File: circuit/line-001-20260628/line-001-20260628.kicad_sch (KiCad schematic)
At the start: 130 parts, among them J1 Conn_01x02_Pin, J2 Conn_01x02_Pin

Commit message: Update ライン基板の回路図を更新
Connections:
- net linesig1 renamed linesig1_{raw}
- net linesig10 renamed linesig10_{raw}
- net linesig11 renamed linesig11_{raw}
- net linesig12 renamed linesig12_{raw}
- net linesig13 renamed linesig13_{raw}
- net linesig14 renamed linesig14_{raw}
- net linesig15 renamed linesig15_{raw}
- net linesig16 renamed linesig16_{raw}
- net linesig17 renamed linesig17_{raw}
- net linesig18 renamed linesig18_{raw}
- net linesig19 renamed linesig19_{raw}
- net linesig2 renamed linesig2_{raw}
- net linesig20 renamed linesig20_{raw}
- net linesig21 renamed linesig21_{raw}
- net linesig22 renamed linesig22_{raw}
- net linesig23 renamed linesig23_{raw}
- net linesig24 renamed linesig24_{raw}
- net linesig25 renamed linesig25_{raw}
- net linesig26 renamed linesig26_{raw}
- net linesig27 renamed linesig27_{raw}
- net linesig28 renamed linesig28_{raw}
- net linesig29 renamed linesig29_{raw}
- net linesig3 renamed linesig3_{raw}
- net linesig30 renamed linesig30_{raw}
- net linesig31 renamed linesig31_{raw}
- net linesig32 renamed linesig32_{raw}
- net linesig4 renamed linesig4_{raw}
- net linesig5 renamed linesig5_{raw}
- net linesig6 renamed linesig6_{raw}
- net linesig7 renamed linesig7_{raw}
- net linesig8 renamed linesig8_{raw}
- net linesig9 renamed linesig9_{raw}

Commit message: Update ラインセンサ基板にコンパレーターを追加（シンボルを作成）
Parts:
- added C1, C2, C3, C4: 10u, symbol Device:C
- added D63, D64, D65, D68: LED, symbol Device:LED
- added D69, D70, D71, D72: D_Photo, symbol Device:D_Photo
- added R63, R64, R65, R68: 10k, symbol Device:R
- added R69, R70, R71, R72: 75, symbol Device:R
- added R73, R74, R75, R76: 1k, symbol Device:R
- added U1, U10, U11, U12, U13, U14, U15, U16, U2, U3, U4, U5, U6, U7, U8, U9: LM339DR, symbol @Thrive_symbol_line:LM393DR
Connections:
- net +5V_{Line}: now also D69.2 (A), D70.2 (A), D71.2 (A), D72.2 (A), R69.2, R70.2, R71.2, R72.2, U1.8 (V_{CC}), U10.8 (V_{CC}), U11.8 (V_{CC}), U12.8 (V_{CC}), U13.8 (V_{CC}), U14.8 (V_{CC}), U15.8 (V_{CC}), U16.8 (V_{CC}), U2.8 (V_{CC}), U3.8 (V_{CC}), U4.8 (V_{CC}), U5.8 (V_{CC}), U6.8 (V_{CC}), U7.8 (V_{CC}), U8.8 (V_{CC}), U9.8 (V_{CC})
- net GND: now also C1.2, C2.2, C3.2, C4.2, D63.1 (K), D64.1 (K), D65.1 (K), D68.1 (K), R63.1, R64.1, R65.1, R68.1, U1.4 (GND), U10.4 (GND), U11.4 (GND), U12.4 (GND), U13.4 (GND), U14.4 (GND), U15.4 (GND), U16.4 (GND), U2.4 (GND), U3.4 (GND), U4.4 (GND), U5.4 (GND), U6.4 (GND), U7.4 (GND), U8.4 (GND), U9.4 (GND)
- net linesig10_{raw}: now also U5.5 (2_{IN+})
- net linesig11_{raw}: now also U6.3 (1_{IN+})
- net linesig12_{raw}: now also U6.5 (2_{IN+})
- net linesig13_{raw}: now also U7.3 (1_{IN+})
- net linesig14_{raw}: now also U7.5 (2_{IN+})
- net linesig15_{raw}: now also U8.3 (1_{IN+})
- net linesig16_{raw}: now also U8.5 (2_{IN+})
- net linesig17_{raw}: now also U9.3 (1_{IN+})
- net linesig18_{raw}: now also U9.5 (2_{IN+})
- net linesig19_{raw}: now also U10.3 (1_{IN+})
- net linesig1_{raw}: now also U1.3 (1_{IN+})
- net linesig20_{raw}: now also U10.5 (2_{IN+})
- net linesig21_{raw}: now also U11.3 (1_{IN+})
- net linesig22_{raw}: now also U11.5 (2_{IN+})
- net linesig23_{raw}: now also U12.3 (1_{IN+})
- net linesig24_{raw}: now also U12.5 (2_{IN+})
- net linesig25_{raw}: now also U13.3 (1_{IN+})
- net linesig26_{raw}: now also U13.5 (2_{IN+})
- net linesig27_{raw}: now also U14.3 (1_{IN+})
- net linesig28_{raw}: now also U14.5 (2_{IN+})
- net linesig29_{raw}: now also U15.3 (1_{IN+})
- net linesig2_{raw}: now also U1.5 (2_{IN+})
- net linesig30_{raw}: now also U15.5 (2_{IN+})
- net linesig31_{raw}: now also U16.3 (1_{IN+})
- net linesig32_{raw}: now also U16.5 (2_{IN+})
- net linesig3_{raw}: now also U2.3 (1_{IN+})
- net linesig4_{raw}: now also U2.5 (2_{IN+})
- net linesig5_{raw}: now also U3.3 (1_{IN+})
- net linesig6_{raw}: now also U3.5 (2_{IN+})
- net linesig7_{raw}: now also U4.3 (1_{IN+})
- net linesig8_{raw}: now also U4.5 (2_{IN+})
- net linesig9_{raw}: now also U5.3 (1_{IN+})
- new net: D63.2 (A), R69.1
- new net: D64.2 (A), R70.1
- new net: D65.2 (A), R71.1
- new net: D68.2 (A), R72.1
- new net boundary_{backleft_raw}: R75.1
- new net boundary_{backleft}: C3.1, R75.2, U10.2 (1_{IN-}), U10.6 (2_{IN-}), U11.2 (1_{IN-}), U11.6 (2_{IN-}), U12.2 (1_{IN-}), U12.6 (2_{IN-}), U9.2 (1_{IN-}), U9.6 (2_{IN-})
- new net boundary_{backright_raw}: R74.1
- new net boundary_{backright}: C2.1, R74.2, U5.2 (1_{IN-}), U5.6 (2_{IN-}), U6.2 (1_{IN-}), U6.6 (2_{IN-}), U7.2 (1_{IN-}), U7.6 (2_{IN-}), U8.2 (1_{IN-}), U8.6 (2_{IN-})
- new net boundary_{frontleft_raw}: R76.1
- new net boundary_{frontleft}: C4.1, R76.2, U13.2 (1_{IN-}), U13.6 (2_{IN-}), U14.2 (1_{IN-}), U14.6 (2_{IN-}), U15.2 (1_{IN-}), U15.6 (2_{IN-}), U16.2 (1_{IN-}), U16.6 (2_{IN-})
- new net boundary_{frontright_raw}: R73.1
- new net boundary_{frontright}: C1.1, R73.2, U1.2 (1_{IN-}), U1.6 (2_{IN-}), U2.2 (1_{IN-}), U2.6 (2_{IN-}), U3.2 (1_{IN-}), U3.6 (2_{IN-}), U4.2 (1_{IN-}), U4.6 (2_{IN-})
- new net linesig10_{digital}: U5.7 (2_{OUT})
- new net linesig11_{digital}: U6.1 (1_{OUT})
- new net linesig12_{digital}: U6.7 (2_{OUT})
- new net linesig13_{digital}: U7.1 (1_{OUT})
- new net linesig14_{digital}: U7.7 (2_{OUT})
- new net linesig15_{digital}: U8.1 (1_{OUT})
- new net linesig16_{digital}: U8.7 (2_{OUT})
- new net linesig17_{digital}: U9.1 (1_{OUT})
- new net linesig18_{digital}: U9.7 (2_{OUT})
- new net linesig19_{digital}: U10.1 (1_{OUT})
- new net linesig1_{digital}: U1.1 (1_{OUT})
- new net linesig20_{digital}: U10.7 (2_{OUT})
- new net linesig21_{digital}: U11.1 (1_{OUT})
- new net linesig22_{digital}: U11.7 (2_{OUT})
- new net linesig23_{digital}: U12.1 (1_{OUT})
- new net linesig24_{digital}: U12.7 (2_{OUT})
- new net linesig25_{digital}: U13.1 (1_{OUT})
- new net linesig26_{digital}: U13.7 (2_{OUT})
- new net linesig27_{digital}: U14.1 (1_{OUT})
- new net linesig28_{digital}: U14.7 (2_{OUT})
- new net linesig29_{digital}: U15.1 (1_{OUT})
- new net linesig2_{digital}: U1.7 (2_{OUT})
- new net linesig30_{digital}: U15.7 (2_{OUT})
- new net linesig31_{digital}: U16.1 (1_{OUT})
- new net linesig32_{digital}: U16.7 (2_{OUT})
- new net linesig33_{analog}: D69.1 (K), R63.2
- new net linesig34_{analog}: D70.1 (K), R64.2
- new net linesig35_{analog}: D71.1 (K), R65.2
- new net linesig36_{analog}: D72.1 (K), R68.2
- new net linesig3_{digital}: U2.1 (1_{OUT})
- new net linesig4_{digital}: U2.7 (2_{OUT})
- new net linesig5_{digital}: U3.1 (1_{OUT})
- new net linesig6_{digital}: U3.7 (2_{OUT})
- new net linesig7_{digital}: U4.1 (1_{OUT})
- new net linesig8_{digital}: U4.7 (2_{OUT})
- new net linesig9_{digital}: U5.1 (1_{OUT})
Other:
- moved on the sheet: J1, J2

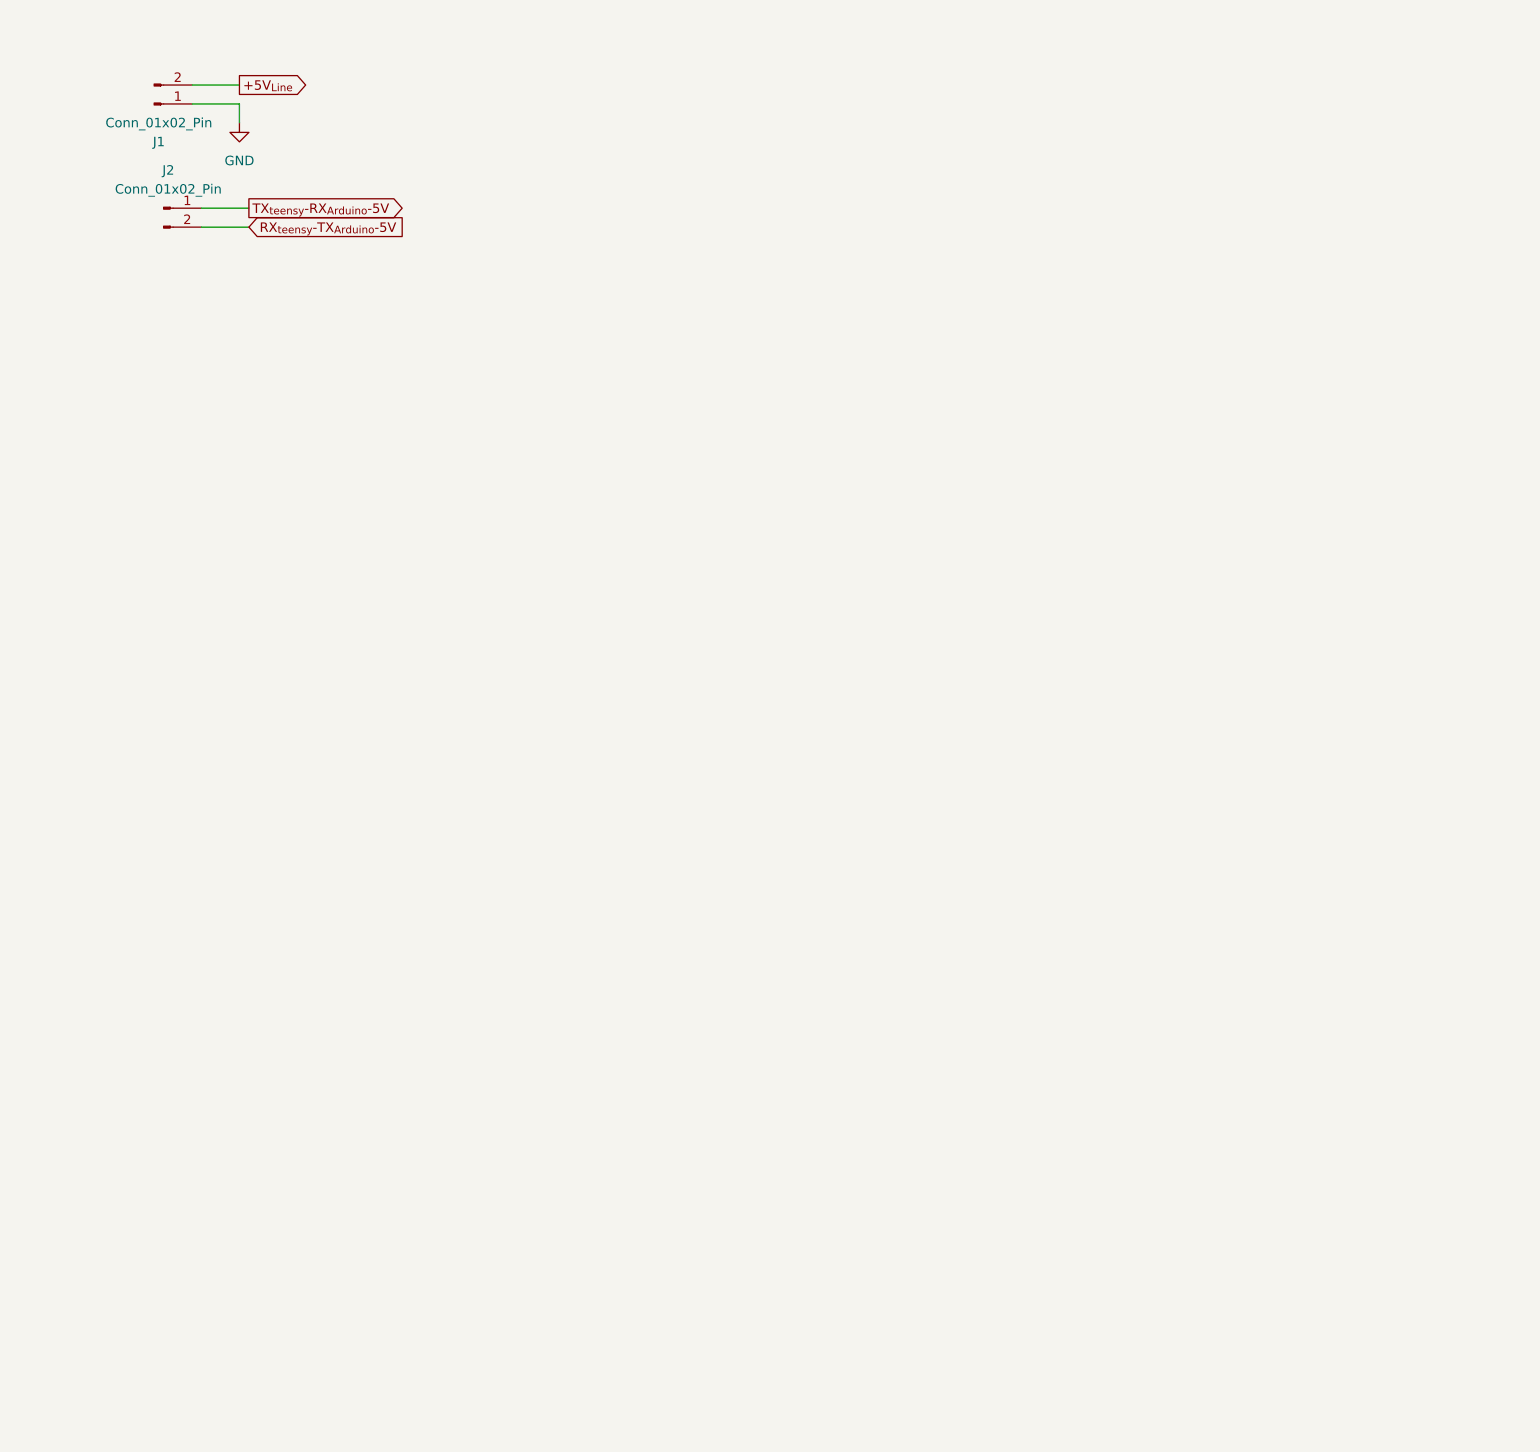
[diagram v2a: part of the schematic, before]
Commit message: Update ラインセンサ基板の回路図を更新
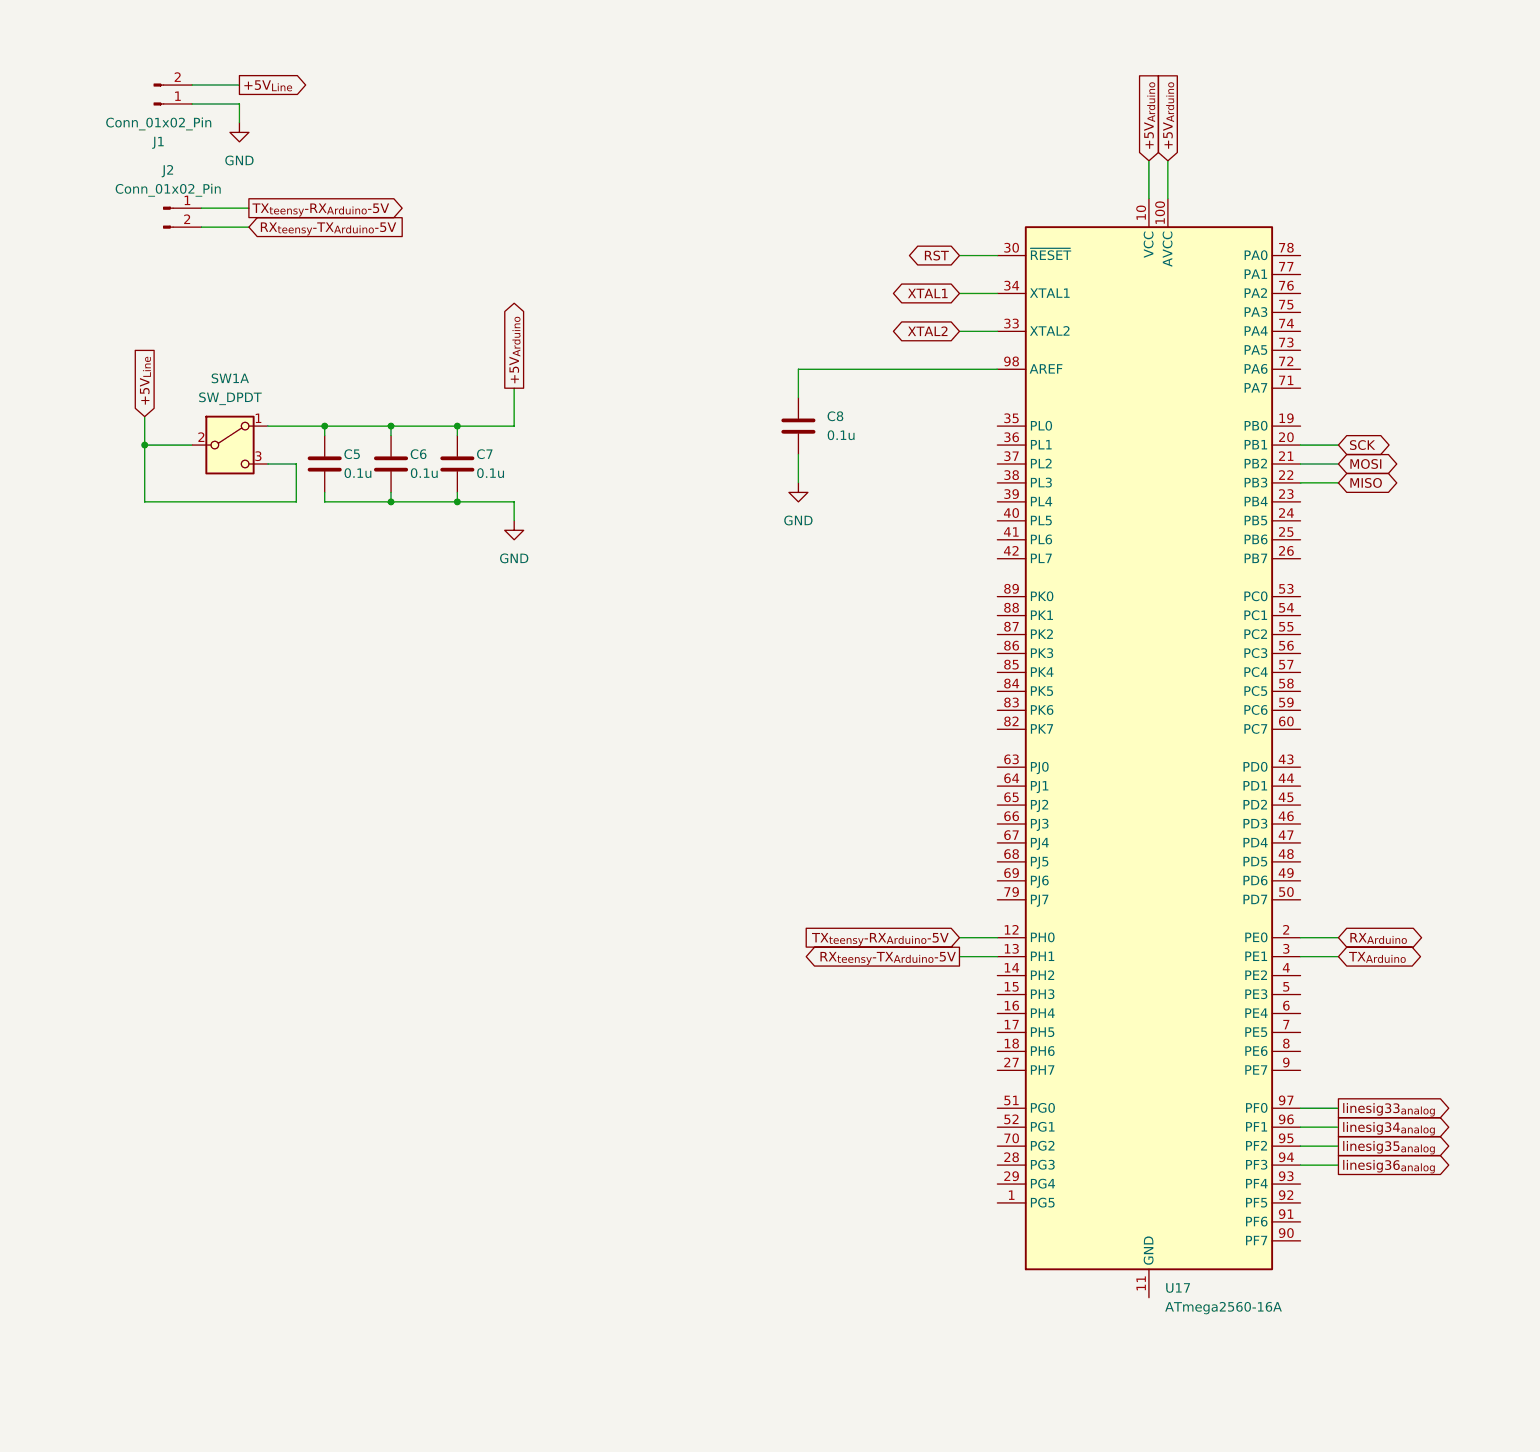
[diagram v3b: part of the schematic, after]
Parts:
- added C5, C6, C7, C8: 0.1u, symbol Device:C
- added SW1: SW_DPDT, symbol Switch:SW_DPDT_x2
- added U17: ATmega2560-16A, Package_QFP:TQFP-100_14x14mm_P0.5mm, symbol MCU_Microchip_ATmega:ATmega2560-16A
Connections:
- net +5V_{Line}: now also SW1.2 (B), SW1.3 (C)
- net GND: now also C5.2, C6.2, C7.2, C8.2
- net RX_{teensy}-TX_{Arduino}-5V: now also U17.13 (PH1)
- net TX_{teensy}-RX_{Arduino}-5V: now also U17.12 (PH0)
- net linesig33_{analog}: now also U17.97 (PF0)
- net linesig34_{analog}: now also U17.96 (PF1)
- net linesig35_{analog}: now also U17.95 (PF2)
- net linesig36_{analog}: now also U17.94 (PF3)
- new net: C8.1, U17.98 (AREF)
- new net: U17.11 (GND), U17.32 (GND), U17.62 (GND), U17.81 (GND), U17.99 (GND)
- new net +5V_{Arduino}: C5.1, C6.1, C7.1, SW1.1 (A), U17.10 (VCC), U17.100 (AVCC), U17.31 (VCC), U17.61 (VCC), U17.80 (VCC)
- new net MISO: U17.22 (PB3)
- new net MOSI: U17.21 (PB2)
- new net RST: U17.30 (~{RESET})
- new net RX_{Arduino}: U17.2 (PE0)
- new net SCK: U17.20 (PB1)
- new net TX_{Arduino}: U17.3 (PE1)
- new net XTAL1: U17.34 (XTAL1)
- new net XTAL2: U17.33 (XTAL2)

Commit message: Update ラインセンサ基板の回路図を更新
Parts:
- added C10, C11, C9: C, symbol Device:C
- added C12: 0.1u, symbol Device:C
- added C13: 10u, symbol Device:C
- added C14: 100u, symbol Device:C
- added J3: Conn_02x03_Odd_Even, symbol Connector_Generic:Conn_02x03_Odd_Even
- added R77: R, symbol Device:R
- added R78: 1M, symbol Device:R
- added SW2: SW_Push, symbol Switch:SW_Push
- added Y1: 16MHz, symbol Device:Crystal
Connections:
- net +5V_{Line}: now also C12.1, C13.1, C14.1, J3.2 (Pin_2), R77.1
- net GND: now also U17.11 (GND), U17.32 (GND), U17.62 (GND), U17.81 (GND), U17.99 (GND), C10.2, C11.2, C12.2, C13.2, C14.2, C9.2, J3.6 (Pin_6), SW2.1
- net MISO: now also J3.1 (Pin_1)
- net MOSI: now also J3.4 (Pin_4)
- net RST: now also C9.1, J3.5 (Pin_5), R77.2, SW2.2
- net SCK: now also J3.3 (Pin_3)
- net XTAL1: now also C11.1, R78.2, Y1.2
- net XTAL2: now also C10.1, R78.1, Y1.1
- net boundary_{backleft_raw}: now also U17.1 (PG5(D4/PWM))
- net boundary_{backright_raw}: now also U17.7 (PE5(D3/PWM))
- net boundary_{frontleft_raw}: now also U17.5 (PE3(D5/PWM))
- net boundary_{frontright_raw}: now also U17.6 (PE4(D2/PWM))
- net linesig10_{digital}: now also U17.63 (PJ0(D15/RX3))
- net linesig11_{digital}: now also U17.46 (PD3(D18/TX1))
- net linesig12_{digital}: now also U17.45 (PD2(D19/RX1))
- net linesig13_{digital}: now also U17.44 (PD1(D20/SDA))
- net linesig14_{digital}: now also U17.43 (PD0(D21/SCL))
- net linesig15_{digital}: now also U17.78 (PA0(D22))
- net linesig16_{digital}: now also U17.77 (PA1(D23))
- net linesig17_{digital}: now also U17.76 (PA2(D24))
- net linesig18_{digital}: now also U17.75 (PA3(D25))
- net linesig19_{digital}: now also U17.74 (PA4(D26))
- net linesig1_{digital}: now also U17.15 (PH3(D6/PWM))
- net linesig20_{digital}: now also U17.73 (PA5(D27))
- net linesig21_{digital}: now also U17.72 (PA6(D28))
- net linesig22_{digital}: now also U17.71 (PA7(D29))
- net linesig23_{digital}: now also U17.60 (PC7(D30))
- net linesig24_{digital}: now also U17.59 (PC6(D31))
- net linesig25_{digital}: now also U17.58 (PC5(D32))
- net linesig26_{digital}: now also U17.57 (PC4(D33))
- net linesig27_{digital}: now also U17.56 (PC3(D34))
- net linesig28_{digital}: now also U17.55 (PC2(D35))
- net linesig29_{digital}: now also U17.54 (PC1(D36))
- net linesig2_{digital}: now also U17.16 (PH4(D7/PWM))
- net linesig30_{digital}: now also U17.53 (PC0(D37))
- net linesig31_{digital}: now also U17.50 (PD7(D38))
- net linesig32_{digital}: now also U17.70 (PG2(D39))
- net linesig3_{digital}: now also U17.17 (PH5(D8/PWM))
- net linesig4_{digital}: now also U17.18 (PH6(D9/PWM))
- net linesig5_{digital}: now also U17.23 (PB4(D10/PWM))
- net linesig6_{digital}: now also U17.24 (PB5(D11/PWM))
- net linesig7_{digital}: now also U17.25 (PB6(D12/PWM))
- net linesig8_{digital}: now also U17.26 (PB7(D13/PWM))
- net linesig9_{digital}: now also U17.64 (PJ1(D14/TX3))
- net LED2: now reaches U17.51 (PG0(D41))
- net LED1: now reaches U17.52 (PG1(D40))
- no-connect marks 0 -> 37
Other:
- moved on the sheet: C1, C2, C3, C4, C5, C6, C7, C8, D1, D10, D11, D12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

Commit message: Update ラインセンサ基板回路図更新
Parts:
- added C15, C16: 22p, symbol Device:C
- added C17, C18, C19: 100n, symbol Device:C
- added P1: USB-typeC, Connector_USB:USB_C_Receptacle_GCT_USB4105-xx-A_16P_TopMnt_Horizontal, symbol Connector:USB_C_Plug
- added R79: 1M, symbol Device:R
- added R80, R81: 22, symbol Device:R
- added R82: 10k, symbol Device:R
- added R83: 5.1k, symbol Device:R
- added U18: CH340G, Package_SO:SOIC-16_3.9x9.9mm_P1.27mm, symbol Interface_USB:CH340G
- added Y2: 12MHz, symbol Device:Crystal
- C9: value C -> 100n
- R77: value R -> 10k
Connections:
- net +5V_{Line}: now also C19.2, U18.16 (VCC)
- net GND: now also C15.1, C16.1, C17.2, C19.1, P1.A1 (GND), P1.A12 (GND), P1.B1 (GND), P1.B12 (GND), R82.2, R83.2, U18.1 (GND)
- net RST: now also C18.2
- net RX_{Arduino}: now also U18.2 (TXD)
- net TX_{Arduino}: now also U18.3 (RXD)
- new net: P1.A6 (D+), R81.1
- new net: C15.2, R79.1, U18.7 (XI), Y2.2
- new net: C16.2, R79.2, U18.8 (XO), Y2.1
- new net: C18.1, R82.1, U18.13 (~{DTR})
- new net: P1.A5 (CC), R83.1
- new net: P1.A4 (VBUS), P1.A9 (VBUS), P1.B4 (VBUS), P1.B9 (VBUS)
- new net: P1.A7 (D-), R80.1
- new net: C17.1, U18.4 (V3)
- new net D+: R81.2, U18.5 (UD+)
- new net D-: R80.2, U18.6 (UD-)
- no-connect marks 37 -> 56
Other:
- moved on the sheet: C1, C10, C11, C12, C13, C14, C2, C3, C4, C5, C6, C7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
